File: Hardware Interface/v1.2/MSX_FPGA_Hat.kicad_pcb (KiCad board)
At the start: 2 copper layers, 103 x 66 mm, 26 parts, among them J1 J1, J2 J2, J3a1 J3a, J3b1 J3b, J4a1 J4a, J4b1 J4b, U1 74LVC245A, U2 74LVC245A, U3 74LVC245A, U4 74LVC245A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

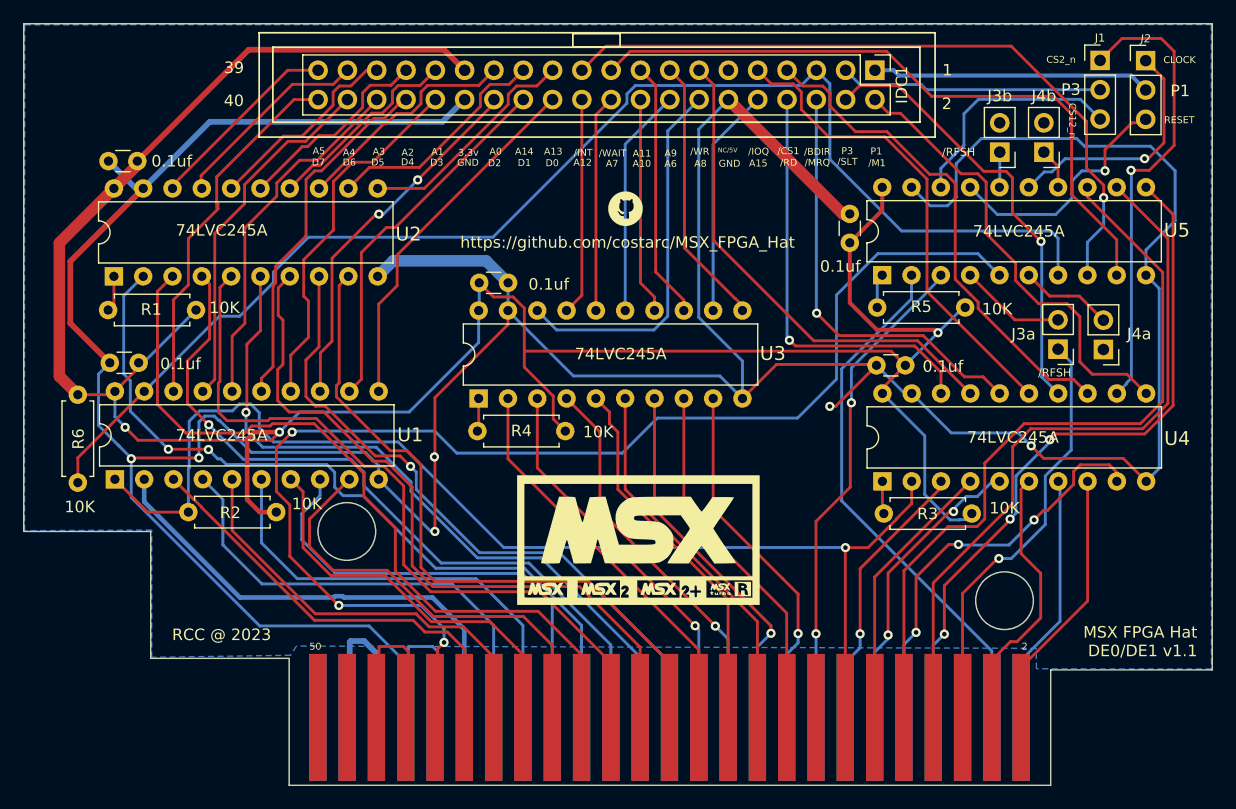
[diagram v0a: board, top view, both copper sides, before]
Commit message: Reverted the interface schema to v1.1, as it's verified that U1 does not need to be driven by its own 7 separate pin.  BUSDIR in the FPGA will continue driving both MSX BUSDIR and U1 DIR pin
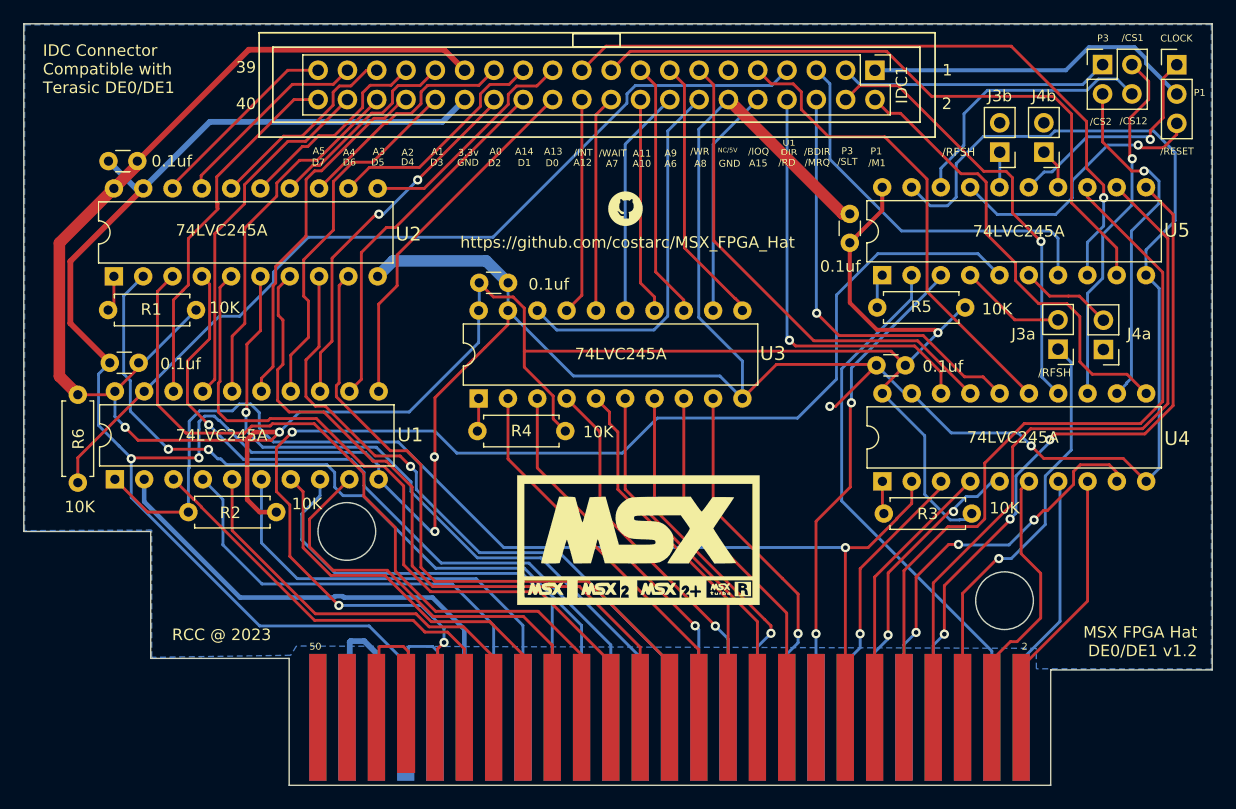
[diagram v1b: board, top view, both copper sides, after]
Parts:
- CONN1: footprint Roni Footprints:MSX_CART -> Roni Footprints:MSX_CART_SW
- J1: footprint Connector_PinHeader_2.54mm:PinHeader_1x03_P2.54mm_Vertical -> Connector_PinHeader_2.54mm:PinHeader_2x02_P2.54mm_Vertical
- moved J2 2.72 mm to (151.9, 23.8)
- moved J1 0.42 mm to (145.4, 23.7)
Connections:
- IDC1 pad 3: C_CS2_CS12 -> /C_CS_SLT
- IDC1 pad 7: /C_CS1 -> /C_LVC245_DIR
- J1 pad 1: /C_CS2 -> /C_CS_SLT
- J1 pad 2: C_CS2_CS12 -> /C_CS1
- J1 pad 3: /C_CS12 -> /C_CS2
- R6 pad 2: /C_BUSDIR -> /C_LVC245_DIR
- U1 pad 19: /C_BUSDIR -> /C_LVC245_DIR
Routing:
- net /C_BUSDIR: track 115.1 -> 34.0 mm
- net /C_LVC245_DIR: track 0.00 -> 78.5 mm
- net /C_CS_SLT: track 0.00 -> 23.5 mm
- net C_CS2_CS12: track 22.8 -> 0.00 mm
- net /C_CS1: track 43.8 -> 31.5 mm, vias 0 -> 1
- net /C_CS2: track 40.3 -> 30.4 mm
- net C_CLK_OR_RST: track 24.2 -> 28.9 mm
- net /C_CS12: track 20.2 -> 23.5 mm
- net /C_RESET: track 21.6 -> 23.8 mm
- net GNDREF: track 358.4 -> 359.9 mm
- net C_CLOCK: track 21.1 -> 19.9 mm
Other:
- board text added: "/CS12"
- board text added: "/CS2"
- board text added: "/RESET"
- board text added: "IDC Connector Compatible with Terasic DE0/DE1"
- board text added: "MSX FPGA Hat DE0/DE1 v1.2"
- board text added: "U1 DIR"
- board text removed: "CS12_n"
- board text removed: "CS2_n"
- board text removed: "MSX FPGA Hat DE0/DE1 v1.1"
- board text removed: "RESET"
